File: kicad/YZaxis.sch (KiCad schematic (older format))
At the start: 31 parts, among them CON16 Stepstick_Left_Connector, CON17 Stepstick_Right_Connector, CON18 Stepstick_Left_Connector, CON19 Stepstick_Right_Connector, Q3 IRLR2905ZPBF, U1 CD40109BPWR

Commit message: Add panel connectors. Minor ERC fixes.
References: #11
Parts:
- gave numbers to parts that had none: 1
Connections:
- no-connect marks 0 -> 7
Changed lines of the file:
@@
 	3400 5950 3400 5100
 $Comp
-L +5V #PWR040
-U 1 1 534EC79A
-P 3400 5100
-F 0 "#PWR040" H 3400 5190 20  0001 C CNN
-F 1 "+5V" H 3390 5240 60  0000 C CNN
-F 2 "~" H 3400 5100 60  0000 C CNN
-F 3 "~" H 3400 5100 60  0000 C CNN
-	1    3400 5100
-	1    0    0    -1
-$EndComp
-$Comp
-L GND #PWR041
+L GND #PWR039
 U 1 1 53470080
 P 3200 6250
-F 0 "#PWR041" H 3200 6250 30  0001 C CNN
+F 0 "#PWR039" H 3200 6250 30  0001 C CNN
 F 1 "GND" H 3200 6180 30  0001 C CNN
 F 2 "~" H 3200 6250 60  0000 C CNN
@@
 $EndComp
 $Comp
-L GND #PWR042
+L GND #PWR040
 U 1 1 53470097
 P 2700 7150
-F 0 "#PWR042" H 2700 7150 30  0001 C CNN
+F 0 "#PWR040" H 2700 7150 30  0001 C CNN
 F 1 "GND" H 2700 7080 30  0001 C CNN
 F 2 "~" H 2700 7150 60  0000 C CNN
@@
 Wire Wire Line
 	2700 6550 2700 6700
-$Comp
-L +5V #PWR043
-U 1 1 534700AA
-P 2000 4650
-F 0 "#PWR043" H 2000 4740 20  0001 C CNN
-F 1 "+5V" H 1990 4790 60  0000 C CNN
-F 2 "~" H 2000 4650 60  0000 C CNN
-F 3 "~" H 2000 4650 60  0000 C CNN
-	1    2000 4650
-	1    0    0    -1
-$EndComp
 Wire Wire Line
 	2000 5050 2000 5350
@@
 Connection ~ 2000 5450
 $Comp
-L GND #PWR044
+L GND #PWR042
 U 1 1 534700CA
 P 2000 7150
-F 0 "#PWR044" H 2000 7150 30  0001 C CNN
+F 0 "#PWR042" H 2000 7150 30  0001 C CNN
 F 1 "GND" H 2000 7080 30  0001 C CNN
 F 2 "~" H 2000 7150 60  0000 C CNN
@@
 Wire Wire Line
 	2000 6950 2000 7150
-$Comp
-L +5V #PWR045
-U 1 1 534700D1
-P 1400 5000
-F 0 "#PWR045" H 1400 5090 20  0001 C CNN
-F 1 "+5V" H 1390 5140 60  0000 C CNN
-F 2 "~" H 1400 5000 60  0000 C CNN
-F 3 "~" H 1400 5000 60  0000 C CNN
-	1    1400 5000
-	1    0    0    -1
-$EndComp
 Wire Wire Line
 	1400 5650 1500 5650
@@
 Y
 $Comp
-L GND #PWR046
+L GND #PWR044
 U 1 1 534EC7A3
 P 8650 5100
-F 0 "#PWR046" H 8650 5100 30  0001 C CNN
+F 0 "#PWR044" H 8650 5100 30  0001 C CNN
 F 1 "GND" H 8650 5030 30  0001 C CNN
 F 2 "~" H 8650 5100 60  0000 C CNN
@@
 $EndComp
 $Comp
-L GND #PWR047
+L GND #PWR045
 U 1 1 534ECB96
 P 10050 4950
-F 0 "#PWR047" H 10050 4950 30  0001 C CNN
+F 0 "#PWR045" H 10050 4950 30  0001 C CNN
 F 1 "GND" H 10050 4880 30  0001 C CNN
 F 2 "~" H 10050 4950 60  0000 C CNN
@@
 $EndComp
 $Comp
-L GND #PWR048
+L GND #PWR046
 U 1 1 534ED3BB
 P 9900 2800
-F 0 "#PWR048" H 9900 2800 30  0001 C CNN
+F 0 "#PWR046" H 9900 2800 30  0001 C CNN
 F 1 "GND" H 9900 2730 30  0001 C CNN
 F 2 "~" H 9900 2800 60  0000 C CNN
@@
 $EndComp
 $Comp
-L GND #PWR049
+L GND #PWR047
 U 1 1 534ED3D4
 P 10500 2800
-F 0 "#PWR049" H 10500 2800 30  0001 C CNN
+F 0 "#PWR047" H 10500 2800 30  0001 C CNN
 F 1 "GND" H 10500 2730 30  0001 C CNN
 F 2 "~" H 10500 2800 60  0000 C CNN
@@
 $EndComp
 $Comp
-L GND #PWR050
+L GND #PWR048
 U 1 1 534ED3DA
 P 9300 2800
-F 0 "#PWR050" H 9300 2800 30  0001 C CNN
+F 0 "#PWR048" H 9300 2800 30  0001 C CNN
 F 1 "GND" H 9300 2730 30  0001 C CNN
 F 2 "~" H 9300 2800 60  0000 C CNN
@@
 	7100 4950 7400 4950
 $Comp
-L GND #PWR051
+L GND #PWR049
 U 1 1 536FED2A
 P 7250 5350
-F 0 "#PWR051" H 7250 5350 30  0001 C CNN
+F 0 "#PWR049" H 7250 5350 30  0001 C CNN
 F 1 "GND" H 7250 5280 30  0001 C CNN
 F 2 "~" H 7250 5350 60  0000 C CNN
@@
 $EndComp
 Wire Wire Line
-	9700 2000 9700 2150
-Wire Wire Line
 	10100 2000 10100 2150
 $Comp
@@
 	3550 2300 3550 1450
 $Comp
-L +5V #PWR052
-U 1 1 537E6253
-P 3550 1450
-F 0 "#PWR052" H 3550 1540 20  0001 C CNN
-F 1 "+5V" H 3540 1590 60  0000 C CNN
-F 2 "~" H 3550 1450 60  0000 C CNN
-F 3 "~" H 3550 1450 60  0000 C CNN
-	1    3550 1450
-	1    0    0    -1
-$EndComp
-$Comp
-L GND #PWR053
+L GND #PWR051
 U 1 1 537E6259
 P 3350 2600
-F 0 "#PWR053" H 3350 2600 30  0001 C CNN
+F 0 "#PWR051" H 3350 2600 30  0001 C CNN
 F 1 "GND" H 3350 2530 30  0001 C CNN
 F 2 "~" H 3350 2600 60  0000 C CNN
@@
 	1    0    0    -1
 $EndComp
-$Comp
-L +5V #PWR054
-U 1 1 537E625F
-P 2150 1200
-F 0 "#PWR054" H 2150 1290 20  0001 C CNN
-F 1 "+5V" H 2140 1340 60  0000 C CNN
-F 2 "~" H 2150 1200 60  0000 C CNN
-F 3 "~" H 2150 1200 60  0000 C CNN
-	1    2150 1200
-	1    0    0    -1
-$EndComp
 Wire Wire Line
 	2150 1500 2150 1700
@@
 Connection ~ 2150 1800
 $Comp
-L GND #PWR055
+L GND #PWR053
 U 1 1 537E626B
 P 2150 3500
-F 0 "#PWR055" H 2150 3500 30  0001 C CNN
+F 0 "#PWR053" H 2150 3500 30  0001 C CNN
 F 1 "GND" H 2150 3430 30  0001 C CNN
 F 2 "~" H 2150 3500 60  0000 C CNN
@@
 Wire Wire Line
 	2150 3500 2150 3200
-$Comp
-L +5V #PWR056
-U 1 1 537E6272
-P 1550 1350
-F 0 "#PWR056" H 1550 1440 20  0001 C CNN
-F 1 "+5V" H 1540 1490 60  0000 C CNN
-F 2 "~" H 1550 1350 60  0000 C CNN
-F 3 "~" H 1550 1350 60  0000 C CNN
-	1    1550 1350
-	1    0    0    -1
-$EndComp
 Wire Wire Line
 	1550 2000 1650 2000
@@
 $EndComp
 $Comp
-L GND #PWR057
+L GND #PWR055
 U 1 1 537E628D
 P 2900 3500
-F 0 "#PWR057" H 2900 3500 30  0001 C CNN
+F 0 "#PWR055" H 2900 3500 30  0001 C CNN
 F 1 "GND" H 2900 3430 30  0001 C CNN
 F 2 "~" H 2900 3500 60  0000 C CNN
@@
 	5600 5050 5600 5150
 $Comp
-L GND #PWR058
+L GND #PWR056
 U 1 1 537E6A4E
 P 5600 5150
-F 0 "#PWR058" H 5600 5150 30  0001 C CNN
+F 0 "#PWR056" H 5600 5150 30  0001 C CNN
 F 1 "GND" H 5600 5080 30  0001 C CNN
 F 2 "~" H 5600 5150 60  0000 C CNN
@@
 	5600 5850 5600 5950
 $Comp
-L GND #PWR059
+L GND #PWR057
 U 1 1 537E6A65
 P 5600 5950
-F 0 "#PWR059" H 5600 5950 30  0001 C CNN
+F 0 "#PWR057" H 5600 5950 30  0001 C CNN
 F 1 "GND" H 5600 5880 30  0001 C CNN
 F 2 "~" H 5600 5950 60  0000 C CNN
@@
 	5600 6650 5600 6750
 $Comp
-L GND #PWR060
+L GND #PWR058
 U 1 1 537E6A80
 P 5600 6750
-F 0 "#PWR060" H 5600 6750 30  0001 C CNN
+F 0 "#PWR058" H 5600 6750 30  0001 C CNN
 F 1 "GND" H 5600 6680 30  0001 C CNN
 F 2 "~" H 5600 6750 60  0000 C CNN
@@
 	5600 7450 5600 7550
 $Comp
-L GND #PWR061
+L GND #PWR059
 U 1 1 537E6A97
 P 5600 7550
-F 0 "#PWR061" H 5600 7550 30  0001 C CNN
+F 0 "#PWR059" H 5600 7550 30  0001 C CNN
 F 1 "GND" H 5600 7480 30  0001 C CNN
 F 2 "~" H 5600 7550 60  0000 C CNN
@@
 	6400 2500 5850 2500
 $Comp
-L +5V #PWR062
-U 1 1 537E6E1C
-P 4750 1700
-F 0 "#PWR062" H 4750 1790 20  0001 C CNN
-F 1 "+5V" H 4740 1840 60  0000 C CNN
-F 2 "~" H 4750 1700 60  0000 C CNN
-F 3 "~" H 4750 1700 60  0000 C CNN
-	1    4750 1700
-	1    0    0    -1
-$EndComp
-$Comp
-L GND #PWR063
+L GND #PWR061
 U 1 1 537E6E27
 P 6650 2200
-F 0 "#PWR063" H 6650 2200 30  0001 C CNN
+F 0 "#PWR061" H 6650 2200 30  0001 C CNN
 F 1 "GND" H 6650 2130 30  0001 C CNN
 F 2 "~" H 6650 2200 60  0000 C CNN
@@
 	4750 1700 4750 2200
 $Comp
-L GND #PWR064
+L GND #PWR062
 U 1 1 537E72EF
 P 4650 2400
-F 0 "#PWR064" H 4650 2400 30  0001 C CNN
+F 0 "#PWR062" H 4650 2400 30  0001 C CNN
 F 1 "GND" H 4650 2330 30  0001 C CNN
 F 2 "~" H 4650 2400 60  0000 C CNN
@@
 Text Label 6400 2000 2    60   ~ 0
 Zmax
-$Comp
-L +5V #PWR065
-U 1 1 537E739F
-P 6550 1700
-F 0 "#PWR065" H 6550 1790 20  0001 C CNN
-F 1 "+5V" H 6540 1840 60  0000 C CNN
-F 2 "~" H 6550 1700 60  0000 C CNN
-F 3 "~" H 6550 1700 60  0000 C CNN
-	1    6550 1700
-	1    0    0    -1
-$EndComp
 Wire Wire Line
 	6650 1800 6650 2200
@@
 	4900 2900 5450 2900
 $Comp
-L CON17x2 CON?
+L CON17x2 CON20
 U 1 1 537E808F
 P 5650 2400
-F 0 "CON?" H 5650 3320 60  0000 C CNN
+F 0 "CON20" H 5650 3320 60  0000 C CNN
 F 1 "YZ" H 5650 1500 60  0000 C CNN
 F 2 "IDC34" H 5650 1400 40  0000 C CNN
@@
 	1    0    0    -1
 $EndComp
+NoConn ~ 8750 2400
+Text GLabel 3550 1450 1    60   UnSpc ~ 0
++5V
+Text GLabel 2150 1200 1    60   UnSpc ~ 0
++5V
+Text GLabel 1550 1350 1    60   UnSpc ~ 0
++5V
+Text GLabel 3400 5100 1    60   UnSpc ~ 0
++5V
+Text GLabel 2000 4650 1    60   UnSpc ~ 0
++5V
+Text GLabel 1400 5000 1    60   UnSpc ~ 0
++5V
+Text GLabel 6550 1700 1    60   UnSpc ~ 0
++5V
+Text GLabel 4750 1700 1    60   UnSpc ~ 0
++5V
+NoConn ~ 5450 3000
+NoConn ~ 5450 3100
+NoConn ~ 5450 3200
+NoConn ~ 5850 3200
+NoConn ~ 5850 3100
+NoConn ~ 5850 3000
+Wire Wire Line
+	9700 2000 9700 2150
 $EndSCHEMATC

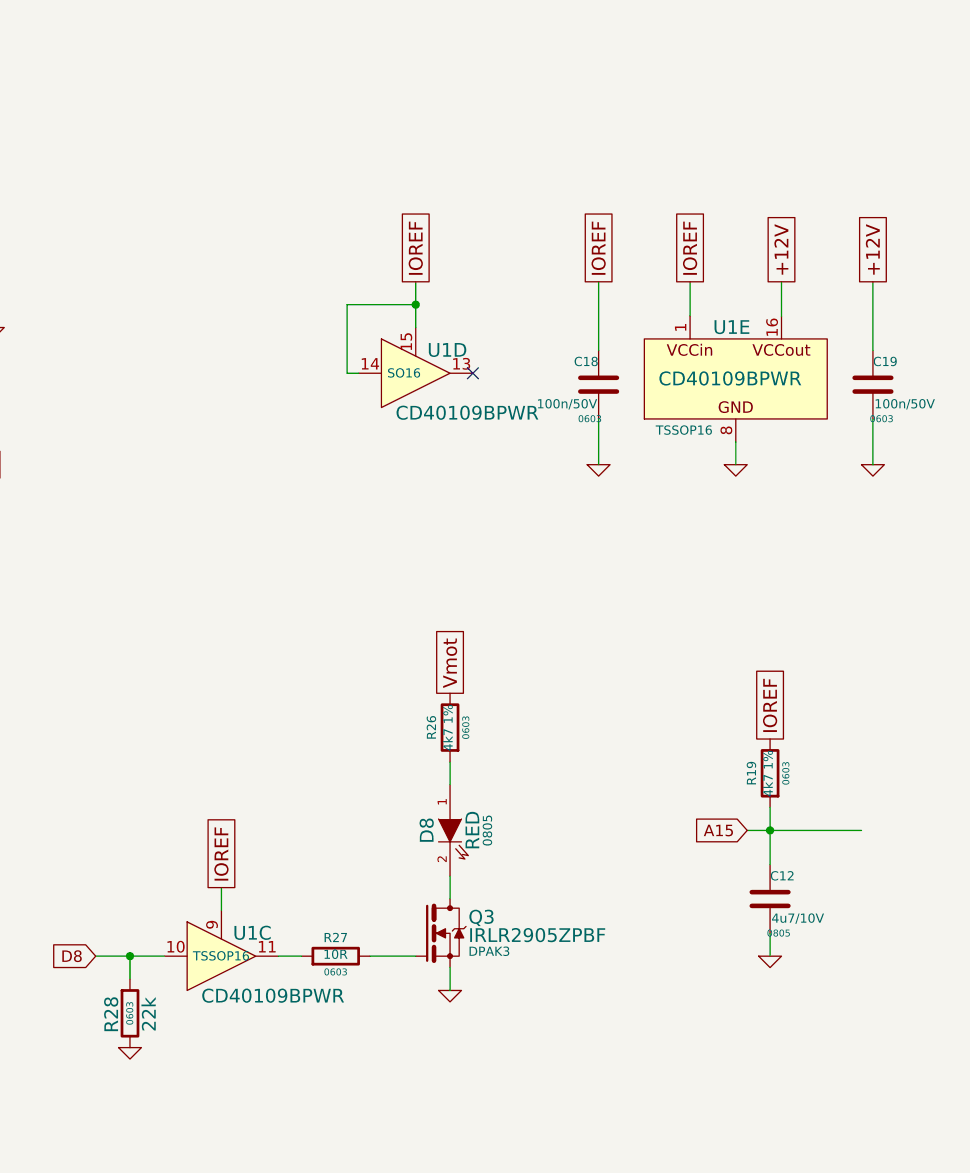
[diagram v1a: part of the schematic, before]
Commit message: Change CD40109 to CD4504
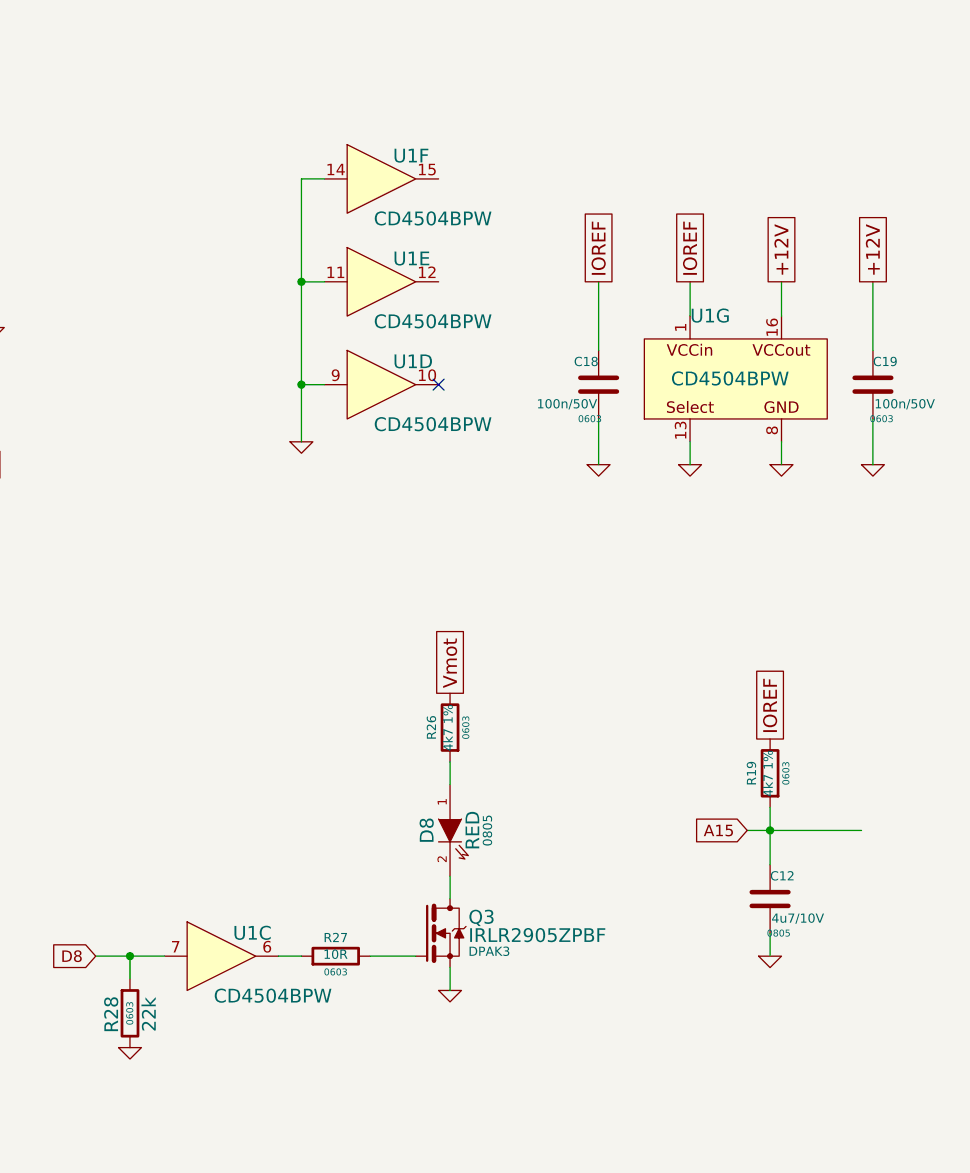
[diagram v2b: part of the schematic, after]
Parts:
- removed U1: CD40109BPWR, TSSOP16, symbol CD40109BPWR
- added U1: CD4504BPW, TSSOP16, symbol CD4504BPW
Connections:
- net +12V: now also U1.16 (VDD)
- net D8: now also U1.7 (IN3)
- net GND: now also U1.11 (IN5), U1.13 (GND), U1.14 (IN6), U1.8 (GND), U1.9 (IN4)
- net IOREF: now also U1.1 (VCC)
- net at R27.1: now also U1.6 (OUT3)
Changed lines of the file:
@@
 	3400 5950 3400 5100
 $Comp
-L GND #PWR039
+L GND #PWR47
 U 1 1 53470080
 P 3200 6250
-F 0 "#PWR039" H 3200 6250 30  0001 C CNN
+F 0 "#PWR47" H 3200 6250 30  0001 C CNN
 F 1 "GND" H 3200 6180 30  0001 C CNN
 F 2 "~" H 3200 6250 60  0000 C CNN
@@
 $EndComp
 $Comp
-L GND #PWR040
+L GND #PWR50
 U 1 1 53470097
 P 2700 7150
-F 0 "#PWR040" H 2700 7150 30  0001 C CNN
+F 0 "#PWR50" H 2700 7150 30  0001 C CNN
 F 1 "GND" H 2700 7080 30  0001 C CNN
 F 2 "~" H 2700 7150 60  0000 C CNN
@@
 Connection ~ 2000 5450
 $Comp
-L GND #PWR042
+L GND #PWR49
 U 1 1 534700CA
 P 2000 7150
-F 0 "#PWR042" H 2000 7150 30  0001 C CNN
+F 0 "#PWR49" H 2000 7150 30  0001 C CNN
 F 1 "GND" H 2000 7080 30  0001 C CNN
 F 2 "~" H 2000 7150 60  0000 C CNN
@@
 Y
 $Comp
-L GND #PWR044
+L GND #PWR43
 U 1 1 534EC7A3
 P 8650 5100
-F 0 "#PWR044" H 8650 5100 30  0001 C CNN
+F 0 "#PWR43" H 8650 5100 30  0001 C CNN
 F 1 "GND" H 8650 5030 30  0001 C CNN
 F 2 "~" H 8650 5100 60  0000 C CNN
@@
 $EndComp
 $Comp
-L GND #PWR045
+L GND #PWR42
 U 1 1 534ECB96
 P 10050 4950
-F 0 "#PWR045" H 10050 4950 30  0001 C CNN
+F 0 "#PWR42" H 10050 4950 30  0001 C CNN
 F 1 "GND" H 10050 4880 30  0001 C CNN
 F 2 "~" H 10050 4950 60  0000 C CNN
@@
 $EndComp
 $Comp
-L GND #PWR046
+L GND #PWR38
 U 1 1 534ED3BB
-P 9900 2800
-F 0 "#PWR046" H 9900 2800 30  0001 C CNN
-F 1 "GND" H 9900 2730 30  0001 C CNN
-F 2 "~" H 9900 2800 60  0000 C CNN
-F 3 "~" H 9900 2800 60  0000 C CNN
-	1    9900 2800
-	1    0    0    -1
-$EndComp
-Wire Wire Line
-	9900 2800 9900 2700
+P 10100 2800
+F 0 "#PWR38" H 10100 2800 30  0001 C CNN
+F 1 "GND" H 10100 2730 30  0001 C CNN
+F 2 "~" H 10100 2800 60  0000 C CNN
+F 3 "~" H 10100 2800 60  0000 C CNN
+	1    10100 2800
+	1    0    0    -1
+$EndComp
+Wire Wire Line
+	10100 2800 10100 2700
 $Comp
 L C C19
@@
 $EndComp
 $Comp
-L GND #PWR047
+L GND #PWR39
 U 1 1 534ED3D4
 P 10500 2800
-F 0 "#PWR047" H 10500 2800 30  0001 C CNN
+F 0 "#PWR39" H 10500 2800 30  0001 C CNN
 F 1 "GND" H 10500 2730 30  0001 C CNN
 F 2 "~" H 10500 2800 60  0000 C CNN
@@
 $EndComp
 $Comp
-L GND #PWR048
+L GND #PWR36
 U 1 1 534ED3DA
 P 9300 2800
-F 0 "#PWR048" H 9300 2800 30  0001 C CNN
+F 0 "#PWR36" H 9300 2800 30  0001 C CNN
 F 1 "GND" H 9300 2730 30  0001 C CNN
 F 2 "~" H 9300 2800 60  0000 C CNN
@@
 	7100 4950 7400 4950
 $Comp
-L GND #PWR049
+L GND #PWR45
 U 1 1 536FED2A
 P 7250 5350
-F 0 "#PWR049" H 7250 5350 30  0001 C CNN
+F 0 "#PWR45" H 7250 5350 30  0001 C CNN
 F 1 "GND" H 7250 5280 30  0001 C CNN
 F 2 "~" H 7250 5350 60  0000 C CNN
@@
 F 3 "~" H 7250 5200 30  0000 C CNN
 	1    7250 5200
-	1    0    0    -1
-$EndComp
-Text GLabel 7650 4650 1    60   UnSpc ~ 0
-IOREF
-Wire Wire Line
-	7650 4650 7650 4750
-$Comp
-L CD40109BPWR U?
-U 3 1 536FED3A
-P 7650 4950
-AR Path="/534454B0/536FED3A" Ref="U?"  Part="2"
-AR Path="/534EC4C7/536FED3A" Ref="U1"  Part="3"
-F 0 "U1" H 7700 5050 60  0000 L CNN
-F 1 "CD40109BPWR" H 7875 4775 60  0000 C CNN
-F 2 "TSSOP16" H 7525 4950 40  0000 L CNN
-F 3 "" H 7500 5550 60  0001 L CNN
-	3    7650 4950
-	1    0    0    -1
-$EndComp
-Text GLabel 8500 2000 1    60   UnSpc ~ 0
-IOREF
-Wire Wire Line
-	8500 2000 8500 2200
-$Comp
-L CD40109BPWR U?
-U 4 1 536FED58
-P 8500 2400
-AR Path="/534454B0/536FED58" Ref="U?"  Part="2"
-AR Path="/534EC4C7/536FED58" Ref="U1"  Part="4"
-F 0 "U1" H 8550 2500 60  0000 L CNN
-F 1 "CD40109BPWR" H 8725 2225 60  0000 C CNN
-F 2 "SO16" H 8375 2400 40  0000 L CNN
-F 3 "" H 8350 3000 60  0001 L CNN
-	4    8500 2400
-	1    0    0    -1
-$EndComp
-Wire Wire Line
-	8250 2400 8200 2400
-Wire Wire Line
-	8200 2400 8200 2100
-Wire Wire Line
-	8200 2100 8500 2100
-Connection ~ 8500 2100
-$Comp
-L CD40109BPWR U?
-U 5 1 536FEDB2
-P 9650 2250
-AR Path="/534454B0/536FEDB2" Ref="U?"  Part="2"
-AR Path="/534EC4C7/536FEDB2" Ref="U1"  Part="5"
-F 0 "U1" H 9800 2300 60  0000 L CNN
-F 1 "CD40109BPWR" H 9875 2075 60  0000 C CNN
-F 2 "TSSOP16" H 9550 1850 40  0000 L CNN
-F 3 "" H 9500 2850 60  0001 L CNN
-	5    9650 2250
 	1    0    0    -1
 $EndComp
@@
 	3550 2300 3550 1450
 $Comp
-L GND #PWR051
+L GND #PWR34
 U 1 1 537E6259
 P 3350 2600
-F 0 "#PWR051" H 3350 2600 30  0001 C CNN
+F 0 "#PWR34" H 3350 2600 30  0001 C CNN
 F 1 "GND" H 3350 2530 30  0001 C CNN
 F 2 "~" H 3350 2600 60  0000 C CNN
@@
 Connection ~ 2150 1800
 $Comp
-L GND #PWR053
+L GND #PWR40
 U 1 1 537E626B
 P 2150 3500
-F 0 "#PWR053" H 2150 3500 30  0001 C CNN
+F 0 "#PWR40" H 2150 3500 30  0001 C CNN
 F 1 "GND" H 2150 3430 30  0001 C CNN
 F 2 "~" H 2150 3500 60  0000 C CNN
@@
 $EndComp
 $Comp
-L GND #PWR055
+L GND #PWR41
 U 1 1 537E628D
 P 2900 3500
-F 0 "#PWR055" H 2900 3500 30  0001 C CNN
+F 0 "#PWR41" H 2900 3500 30  0001 C CNN
 F 1 "GND" H 2900 3430 30  0001 C CNN
 F 2 "~" H 2900 3500 60  0000 C CNN
@@
 	5600 5050 5600 5150
 $Comp
-L GND #PWR056
+L GND #PWR44
 U 1 1 537E6A4E
 P 5600 5150
-F 0 "#PWR056" H 5600 5150 30  0001 C CNN
+F 0 "#PWR44" H 5600 5150 30  0001 C CNN
 F 1 "GND" H 5600 5080 30  0001 C CNN
 F 2 "~" H 5600 5150 60  0000 C CNN
@@
 	5600 5850 5600 5950
 $Comp
-L GND #PWR057
+L GND #PWR46
 U 1 1 537E6A65
 P 5600 5950
-F 0 "#PWR057" H 5600 5950 30  0001 C CNN
+F 0 "#PWR46" H 5600 5950 30  0001 C CNN
 F 1 "GND" H 5600 5880 30  0001 C CNN
 F 2 "~" H 5600 5950 60  0000 C CNN
@@
 	5600 6650 5600 6750
 $Comp
-L GND #PWR058
+L GND #PWR48
 U 1 1 537E6A80
 P 5600 6750
-F 0 "#PWR058" H 5600 6750 30  0001 C CNN
+F 0 "#PWR48" H 5600 6750 30  0001 C CNN
 F 1 "GND" H 5600 6680 30  0001 C CNN
 F 2 "~" H 5600 6750 60  0000 C CNN
@@
 	5600 7450 5600 7550
 $Comp
-L GND #PWR059
+L GND #PWR51
 U 1 1 537E6A97
 P 5600 7550
-F 0 "#PWR059" H 5600 7550 30  0001 C CNN
+F 0 "#PWR51" H 5600 7550 30  0001 C CNN
 F 1 "GND" H 5600 7480 30  0001 C CNN
 F 2 "~" H 5600 7550 60  0000 C CNN
@@
 	6400 2500 5850 2500
 $Comp
-L GND #PWR061
+L GND #PWR32
 U 1 1 537E6E27
 P 6650 2200
-F 0 "#PWR061" H 6650 2200 30  0001 C CNN
+F 0 "#PWR32" H 6650 2200 30  0001 C CNN
 F 1 "GND" H 6650 2130 30  0001 C CNN
 F 2 "~" H 6650 2200 60  0000 C CNN
@@
 	4750 1700 4750 2200
 $Comp
-L GND #PWR062
+L GND #PWR33
 U 1 1 537E72EF
 P 4650 2400
-F 0 "#PWR062" H 4650 2400 30  0001 C CNN
+F 0 "#PWR33" H 4650 2400 30  0001 C CNN
 F 1 "GND" H 4650 2330 30  0001 C CNN
 F 2 "~" H 4650 2400 60  0000 C CNN
@@
 	1    0    0    -1
 $EndComp
-NoConn ~ 8750 2400
+NoConn ~ 8600 2450
 Text GLabel 3550 1450 1    60   UnSpc ~ 0
 +5V
@@
 Wire Wire Line
 	9700 2000 9700 2150
+$Comp
+L CD4504BPW U1
+U 3 1 538D6C83
+P 7650 4950
+F 0 "U1" H 7700 5050 60  0000 L CNN
+F 1 "CD4504BPW" H 7875 4775 60  0000 C CNN
+F 2 "TSSOP16" H 7525 4950 40  0001 L CNN
+F 3 "" H 7500 5550 60  0001 L CNN
+	3    7650 4950
+	1    0    0    -1
+$EndComp
+$Comp
+L CD4504BPW U1
+U 4 1 538D6CCE
+P 8350 2450
+F 0 "U1" H 8400 2550 60  0000 L CNN
+F 1 "CD4504BPW" H 8575 2275 60  0000 C CNN
+F 2 "TSSOP16" H 8225 2450 40  0001 L CNN
+F 3 "" H 8200 3050 60  0001 L CNN
+	4    8350 2450
+	1    0    0    -1
+$EndComp
+$Comp
+L CD4504BPW U1
+U 5 1 538D6D2F
+P 8350 2000
+F 0 "U1" H 8400 2100 60  0000 L CNN
+F 1 "CD4504BPW" H 8575 1825 60  0000 C CNN
+F 2 "TSSOP16" H 8225 2000 40  0001 L CNN
+F 3 "" H 8200 2600 60  0001 L CNN
+	5    8350 2000
+	1    0    0    -1
+$EndComp
+$Comp
+L CD4504BPW U1
+U 6 1 538D6D88
+P 8350 1550
+F 0 "U1" H 8400 1650 60  0000 L CNN
+F 1 "CD4504BPW" H 8575 1375 60  0000 C CNN
+F 2 "TSSOP16" H 8225 1550 40  0001 L CNN
+F 3 "" H 8200 2150 60  0001 L CNN
+	6    8350 1550
+	1    0    0    -1
+$EndComp
+$Comp
+L CD4504BPW U1
+U 7 1 538D6DF7
+P 9650 2250
+F 0 "U1" H 9700 2350 60  0000 L CNN
+F 1 "CD4504BPW" H 9875 2075 60  0000 C CNN
+F 2 "TSSOP16" H 9525 2250 40  0001 L CNN
+F 3 "" H 9500 2850 60  0001 L CNN
+	7    9650 2250
+	1    0    0    -1
+$EndComp
+Wire Wire Line
+	8100 1550 8000 1550
+Wire Wire Line
+	8000 1550 8000 2700
+Wire Wire Line
+	8100 2450 8000 2450
+Connection ~ 8000 2450
+Wire Wire Line
+	8100 2000 8000 2000
+Connection ~ 8000 2000
+$Comp
+L GND #PWR35
+U 1 1 538D7812
+P 8000 2700
+F 0 "#PWR35" H 8000 2700 30  0001 C CNN
+F 1 "GND" H 8000 2630 30  0001 C CNN
+F 2 "~" H 8000 2700 60  0000 C CNN
+F 3 "~" H 8000 2700 60  0000 C CNN
+	1    8000 2700
+	1    0    0    -1
+$EndComp
+$Comp
+L GND #PWR37
+U 1 1 538D791A
+P 9700 2800
+F 0 "#PWR37" H 9700 2800 30  0001 C CNN
+F 1 "GND" H 9700 2730 30  0001 C CNN
+F 2 "~" H 9700 2800 60  0000 C CNN
+F 3 "~" H 9700 2800 60  0000 C CNN
+	1    9700 2800
+	1    0    0    -1
+$EndComp
+Wire Wire Line
+	9700 2800 9700 2700
 $EndSCHEMATC
